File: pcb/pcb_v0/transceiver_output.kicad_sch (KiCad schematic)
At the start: 26 parts, among them J1 Conn_01x02_Pin, J2 Conn_01x02_Pin, J3 Conn_01x02_Pin, J4 Conn_01x02_Pin, U1 MAX3221EIPWR

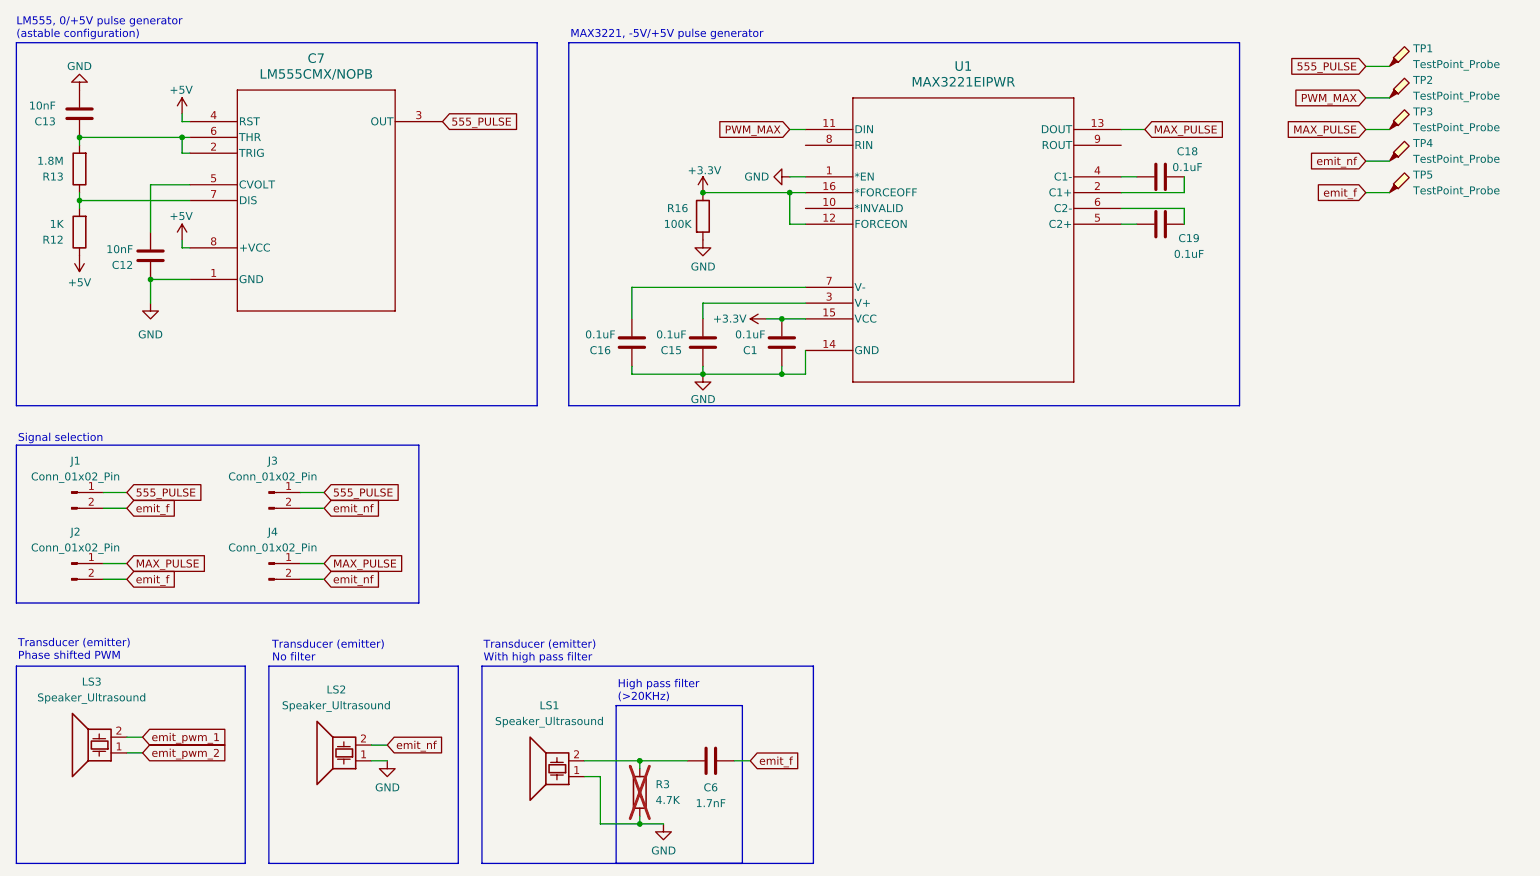
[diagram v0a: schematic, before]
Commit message: fix(pcb): update design to match teacher requirements
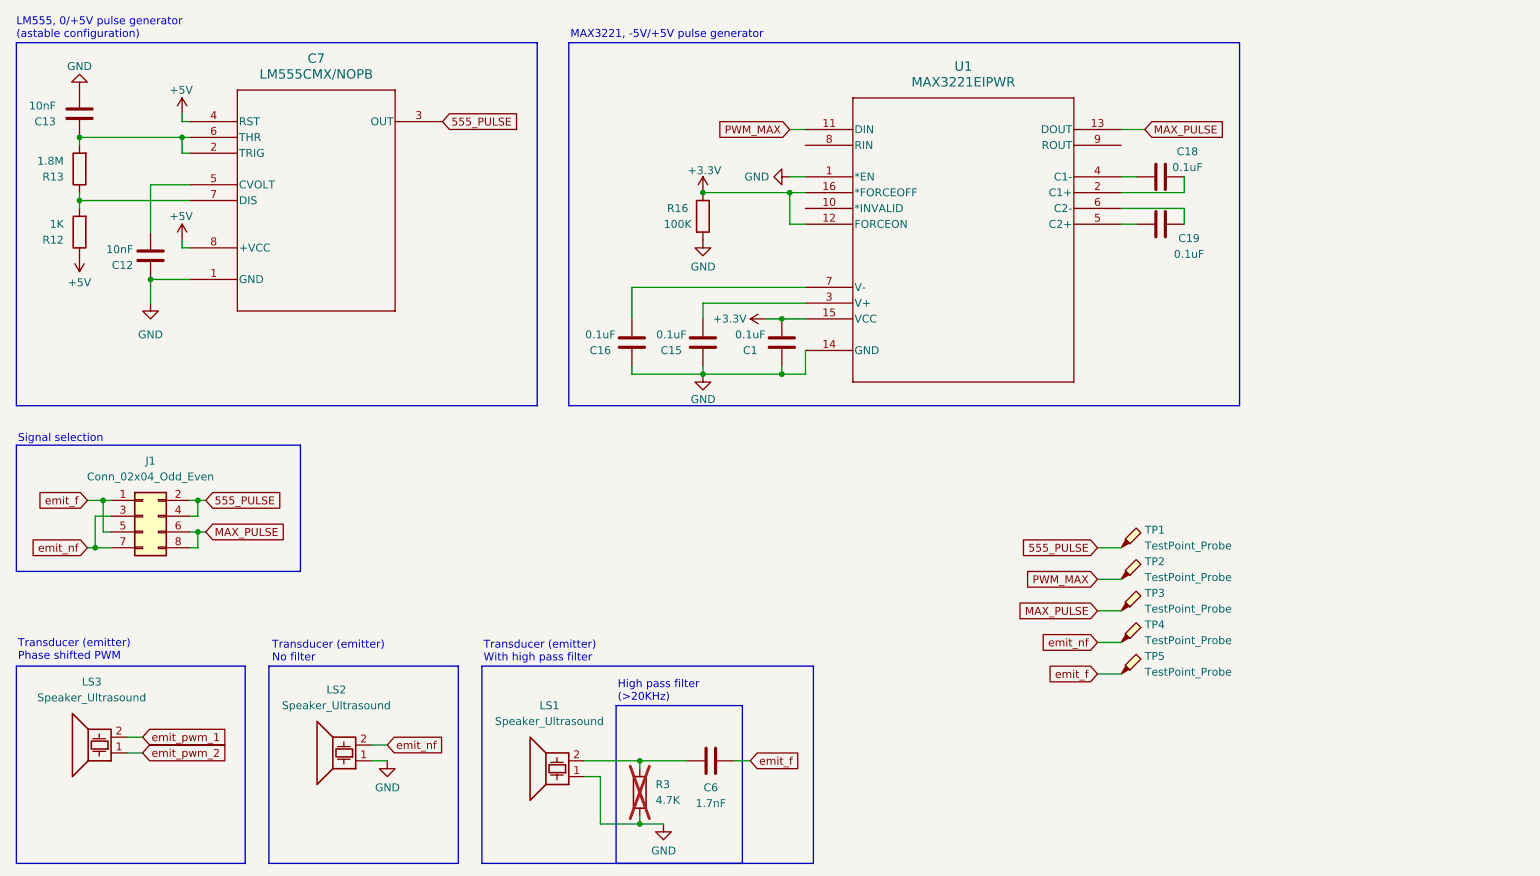
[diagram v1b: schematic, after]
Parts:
- removed J1, J2, J3, J4: Conn_01x02_Pin, Connector_PinHeader_2.54mm:PinHeader_1x02_P2.54mm_Vertical, symbol Connector:Conn_01x02_Pin
- added J1: Conn_02x04_Odd_Even, Connector_PinHeader_2.54mm:PinHeader_2x04_P2.54mm_Vertical, symbol Connector_Generic:Conn_02x04_Odd_Even
- C1, C12, C13, C15, C16, C18, C19, C6: footprint Capacitor_THT:C_Disc_D3.0mm_W1.6mm_P2.50mm -> Capacitor_THT:C_Disc_D4.3mm_W1.9mm_P5.00mm
- R12, R13, R16, R3: footprint Resistor_THT:R_Axial_DIN0204_L3.6mm_D1.6mm_P5.08mm_Horizontal -> Resistor_THT:R_Axial_DIN0207_L6.3mm_D2.5mm_P10.16mm_Horizontal
- TP1, TP2, TP3, TP4, TP5: footprint TestPoint:TestPoint_THTPad_1.0x1.0mm_Drill0.5mm -> TestPoint:TestPoint_THTPad_3.0x3.0mm_Drill1.5mm
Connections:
- net 555_PULSE: now also J1.2 (Pin_2), J1.4 (Pin_4)
- net MAX_PULSE: now also J1.6 (Pin_6), J1.8 (Pin_8)
- net emit_f: now also J1.1 (Pin_1), J1.5 (Pin_5)
- net emit_nf: now also J1.3 (Pin_3), J1.7 (Pin_7)
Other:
- moved on the sheet: TP1, TP2, TP3, TP4, TP5
